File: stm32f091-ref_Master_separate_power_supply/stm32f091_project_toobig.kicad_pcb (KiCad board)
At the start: 2 copper layers, 83.8 x 130.8 mm, 62 parts, among them J1 Conn_02x05_Odd_Even, J2 Conn_01x08_Female, J3 Conn_01x02_Female, J4 Conn_01x09_Female, SW1 SW_Push, U1 LD1117S33TR_SOT223, U2 LM324, U3 STM32F091RCTx, U4 LM386

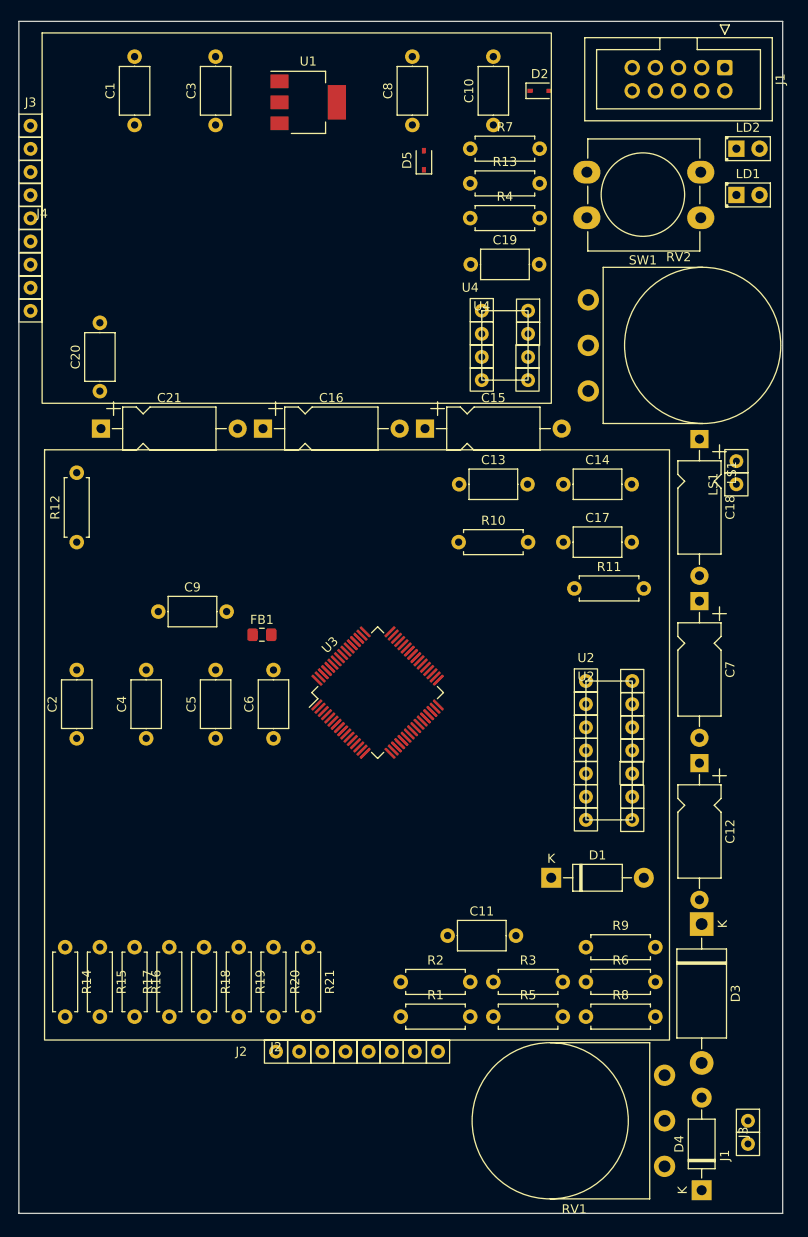
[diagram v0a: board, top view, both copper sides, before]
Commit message: PCB designs w/out traces for a regular and condensed PCB
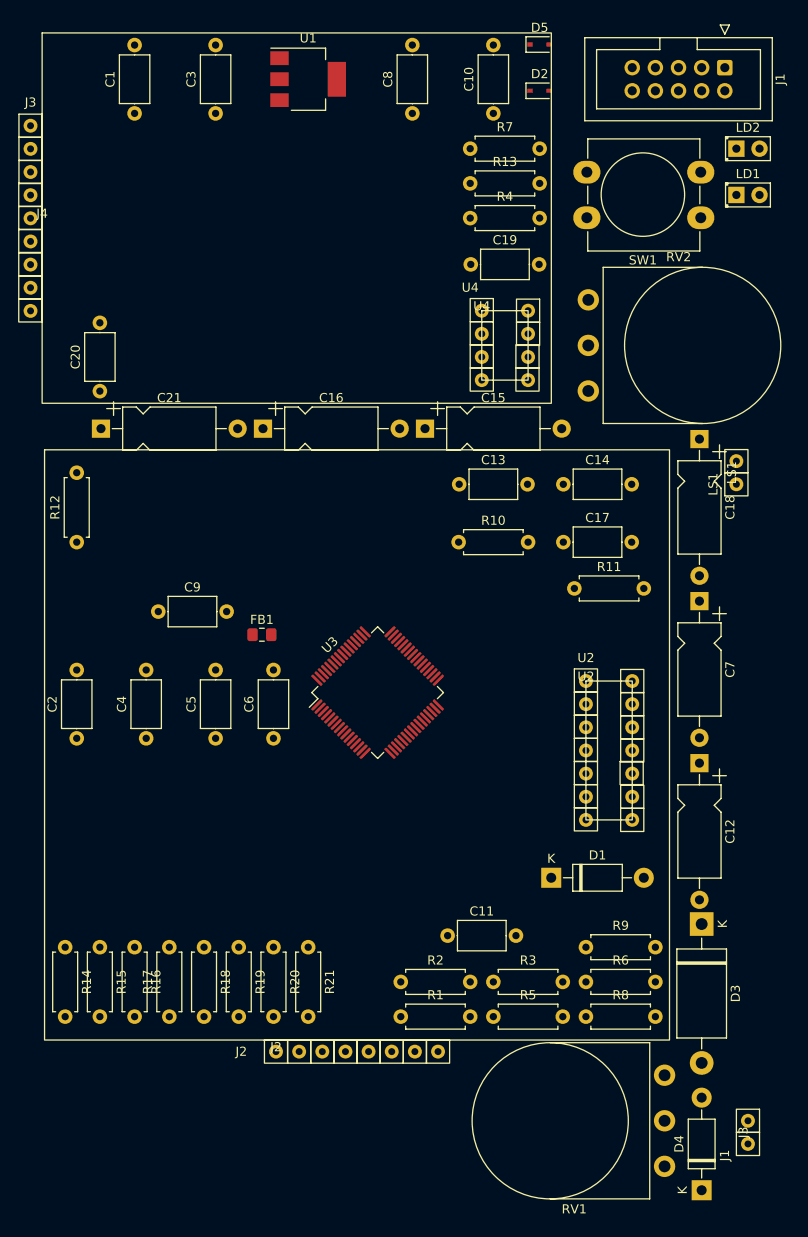
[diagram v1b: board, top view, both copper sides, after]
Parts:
- moved D5 18.0 mm to (147.3, 24.1), turned to 0 degrees
- moved U1 2.54 mm to (121.9, 27.9)
- moved C1 1.27 mm to (102.9, 31.6)
- moved C10 1.27 mm to (142.3, 31.6)
- moved C3 1.27 mm to (111.8, 31.6)
- moved C8 1.27 mm to (133.4, 31.6)
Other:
- board outline removed
- copper layers 2 -> 4
- rule pad_to_mask_clearance: 0.0508 -> 0.05
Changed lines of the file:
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@@
 (kicad_pcb (version 20211014) (generator pcbnew)
   (general
-    (thickness 0.57)
+    (thickness 1.6)
   )
   (paper "A4")
@@
   (layers
     (0 "F.Cu" signal)
+    (1 "In1.Cu" signal "Ground.Cu")
+    (2 "In2.Cu" signal "Power.Cu")
     (31 "B.Cu" signal)
+    (32 "B.Adhes" user "B.Adhesive")
+    (33 "F.Adhes" user "F.Adhesive")
     (34 "B.Paste" user)
     (35 "F.Paste" user)
@@
     (40 "Dwgs.User" user "User.Drawings")
     (41 "Cmts.User" user "User.Comments")
+    (42 "Eco1.User" user "User.Eco1")
+    (43 "Eco2.User" user "User.Eco2")
     (44 "Edge.Cuts" user)
     (45 "Margin" user)
     (46 "B.CrtYd" user "B.Courtyard")
     (47 "F.CrtYd" user "F.Courtyard")
+    (48 "B.Fab" user)
     (49 "F.Fab" user)
   )
   (setup
-    (stackup
-      (layer "F.SilkS" (type "Top Silk Screen"))
-      (layer "F.Paste" (type "Top Solder Paste"))
-      (layer "F.Mask" (type "Top Solder Mask") (thickness 0.01))
-      (layer "F.Cu" (type "copper") (thickness 0.035))
-      (layer "dielectric 1" (type "core") (thickness 0.48) (material "FR4") (epsilon_r 4.5) (loss_tangent 0.02))
-      (layer "B.Cu" (type "copper") (thickness 0.035))
-      (layer "B.Mask" (type "Bottom Solder Mask") (thickness 0.01))
-      (layer "B.Paste" (type "Bottom Solder Paste"))
-      (layer "B.SilkS" (type "Bottom Silk Screen"))
-      (copper_finish "None")
-      (dielectric_constraints no)
-    )
-    (pad_to_mask_clearance 0.0508)
-    (solder_mask_min_width 0.101)
+    (pad_to_mask_clearance 0.05)
     (grid_origin 99.07762 130.73476)
     (pcbplotparams
@@
   )
   (footprint "Diode_SMD:D_SOD-323" (layer "F.Cu")
-    (at 134.63762 36.75476 90)
+    (at 147.33762 24.05476)
     (descr "SOD-323")
     (tags "SOD-323")
@@
     (property "Sheetname" "")
     (attr smd)
-    (fp_text reference "D5" (at 0 -1.85 90) (layer "F.SilkS")
+    (fp_text reference "D5" (at 0 -1.85) (layer "F.SilkS")
       (effects (font (size 1 1) (thickness 0.15)))
     )
-    (fp_text value "BAT60JFILM" (at 0.1 1.9 90) (layer "F.Fab")
+    (fp_text value "BAT60JFILM" (at 0.1 1.9) (layer "F.Fab")
       (effects (font (size 1 1) (thickness 0.15)))
     )
-    (fp_text user "${REFERENCE}" (at 0 -1.85 90) (layer "F.Fab")
+    (fp_text user "${REFERENCE}" (at 0 -1.85) (layer "F.Fab")
       (effects (font (size 1 1) (thickness 0.15)))
     )
@@
     (fp_line (start -0.3 -0.35) (end -0.3 0.35) (layer "F.Fab") (width 0.1))
     (fp_line (start 0.9 0.7) (end -0.9 0.7) (layer "F.Fab") (width 0.1))
-    (pad "1" smd rect (at -1.05 0 90) (size 0.6 0.45) (layers "F.Cu" "F.Paste" "F.Mask")
+    (pad "1" smd rect (at -1.05 0) (size 0.6 0.45) (layers "F.Cu" "F.Paste" "F.Mask")
       (net 12 "+3V0") (pinfunction "K") (pintype "passive"))
-    (pad "2" smd rect (at 1.05 0 90) (size 0.6 0.45) (layers "F.Cu" "F.Paste" "F.Mask")
+    (pad "2" smd rect (at 1.05 0) (size 0.6 0.45) (layers "F.Cu" "F.Paste" "F.Mask")
       (net 46 "Net-(C10-Pad1)") (pinfunction "A") (pintype "passive"))
     (model "${KICAD6_3DMODEL_DIR}/Diode_SMD.3dshapes/D_SOD-323.wrl"
@@
   )
   (footprint "Capacitor_THT:C_Axial_L5.1mm_D3.1mm_P7.50mm_Horizontal" (layer "F.Cu")
-    (at 102.88762 32.88476 90)
+    (at 102.88762 31.61476 90)
     (descr "C, Axial series, Axial, Horizontal, pin pitch=7.5mm, , length*diameter=5.1*3.1mm^2, http://www.vishay.com/docs/45231/arseries.pdf")
     (tags "C Axial series Axial Horizontal pin pitch 7.5mm  length 5.1mm diameter 3.1mm")
@@
   )
   (footprint "Capacitor_THT:C_Axial_L5.1mm_D3.1mm_P7.50mm_Horizontal" (layer "F.Cu")
-    (at 111.77762 32.88476 90)
+    (at 111.77762 31.61476 90)
     (descr "C, Axial series, Axial, Horizontal, pin pitch=7.5mm, , length*diameter=5.1*3.1mm^2, http://www.vishay.com/docs/45231/arseries.pdf")
     (tags "C Axial series Axial Horizontal pin pitch 7.5mm  length 5.1mm diameter 3.1mm")
@@
   )
   (footprint "Package_TO_SOT_SMD:SOT-223-3_TabPin2" (layer "F.Cu")
-    (at 121.93762 30.40476)
+    (at 121.93762 27.86476)
     (descr "module CMS SOT223 4 pins")
     (tags "CMS SOT")
@@
   )
   (footprint "Capacitor_THT:C_Axial_L5.1mm_D3.1mm_P7.50mm_Horizontal" (layer "F.Cu")
-    (at 133.36762 32.88476 90)
+    (at 133.36762 31.61476 90)
     (descr "C, Axial series, Axial, Horizontal, pin pitch=7.5mm, , length*diameter=5.1*3.1mm^2, http://www.vishay.com/docs/45231/arseries.pdf")
     (tags "C Axial series Axial Horizontal pin pitch 7.5mm  length 5.1mm diameter 3.1mm")
@@
   )
   (footprint "Capacitor_THT:C_Axial_L5.1mm_D3.1mm_P7.50mm_Horizontal" (layer "F.Cu")
-    (at 142.25762 32.88476 90)
+    (at 142.25762 31.61476 90)
     (descr "C, Axial series, Axial, Horizontal, pin pitch=7.5mm, , length*diameter=5.1*3.1mm^2, http://www.vishay.com/docs/45231/arseries.pdf")
     (tags "C Axial series Axial Horizontal pin pitch 7.5mm  length 5.1mm diameter 3.1mm")
@@
     )
   )
-  (gr_line (start 90.18762 21.51476) (end 174.00762 21.51476) (layer "Edge.Cuts") (width 0.0254))
-  (gr_line (start 174.00762 21.51476) (end 174.00762 152.32476) (layer "Edge.Cuts") (width 0.0254))
-  (gr_line (start 90.18762 152.32476) (end 90.18762 21.51476) (layer "Edge.Cuts") (width 0.0254))
-  (gr_line (start 174.00762 152.32476) (end 90.18762 152.32476) (layer "Edge.Cuts") (width 0.0254))
 )

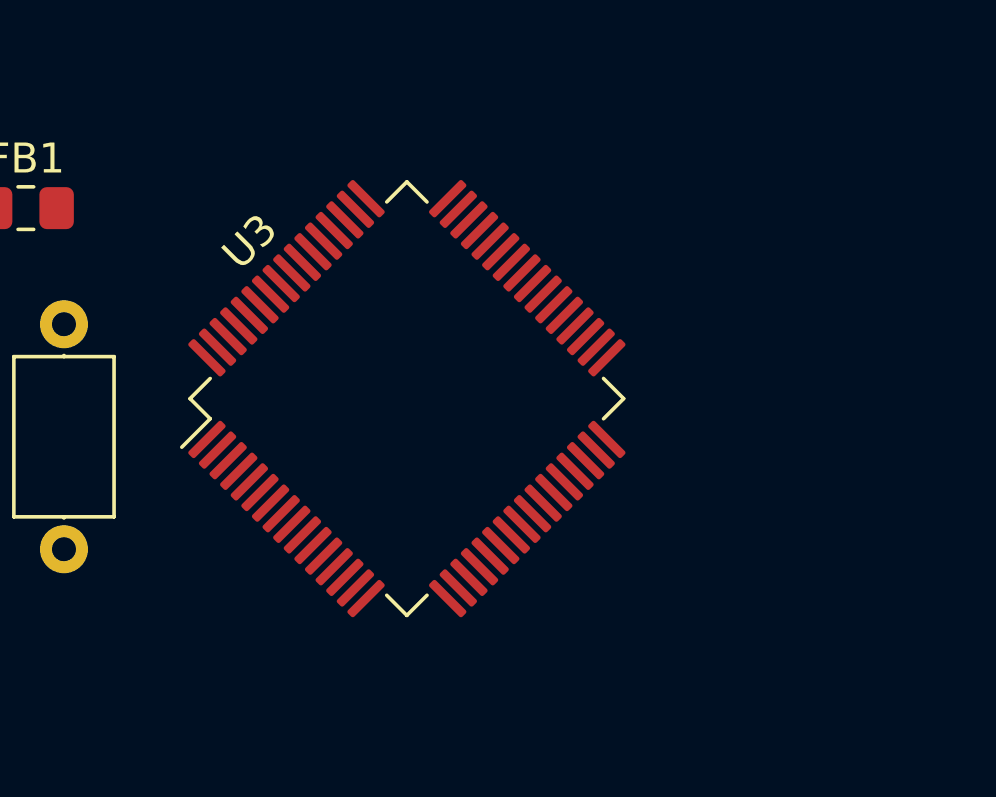
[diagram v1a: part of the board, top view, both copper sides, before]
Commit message: changed r's and c's to SM in condensed PCB design
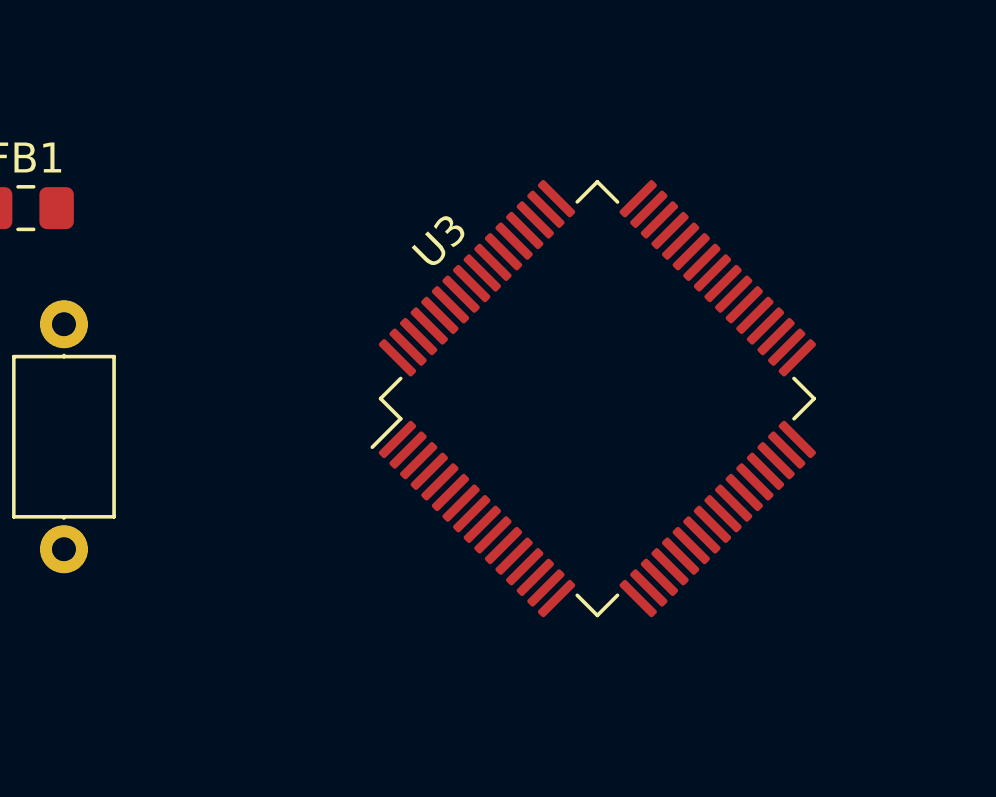
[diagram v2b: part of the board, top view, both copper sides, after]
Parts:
- moved U3 6.35 mm to (135.9, 95.2)
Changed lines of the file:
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@@
   )
   (footprint "Package_QFP:LQFP-64_10x10mm_P0.5mm" (layer "F.Cu")
-    (at 129.55762 95.17476 45)
+    (at 135.90762 95.17476 45)
     (descr "LQFP, 64 Pin (https://www.analog.com/media/en/technical-documentation/data-sheets/ad7606_7606-6_7606-4.pdf), generated with kicad-footprint-generator ipc_gullwing_generator.py")
     (tags "LQFP QFP")
